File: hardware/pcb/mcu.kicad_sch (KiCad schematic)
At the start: 14 parts, among them J3 FSR pads, U1 ESP32-WROOM-32E-N8R2, U18 W25Q512JVEIQ, U19 TCA6408ARSVR

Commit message: Fix the review's datasheet errors without changing respiration or the GDTs.
Replace the MCP73831 with a BQ25170 so a flat cell still charges from USB, add the missing series protection and ESP32/CP2102 passives, and withdraw the claim that respiration still works with 51 kΩ in the loop.

Co-authored-by: Riyu-D1 <Riyu-D1@users.noreply.github.com>
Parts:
- added C64: 1u, Capacitor_SMD:C_0402_1005Metric, symbol vitalq:C
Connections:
- net +3V3: no longer U19.1 (~{RESET})
- net ESP_EN: now also U19.1 (~{RESET}), C64.1
- net GND: now also C64.2
- net GAUGE_ALRT: now reaches U1.10 (IO25)
- net CHG_PG: now reaches U1.12 (IO27)
- net CHG_EN renamed CHG_DIS
- net NTC_ADC: no longer names the net of U1.5 (SENSOR_VN)
- no-connect marks 5 -> 4
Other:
- note added: "EN has R5 10k and C64 1 uF. Q3 on the USB sheet is the DTR/RTS auto-program pair."
- note removed: "EN and IO0 have pull-ups only. Download uses the module pads. There are no buttons."

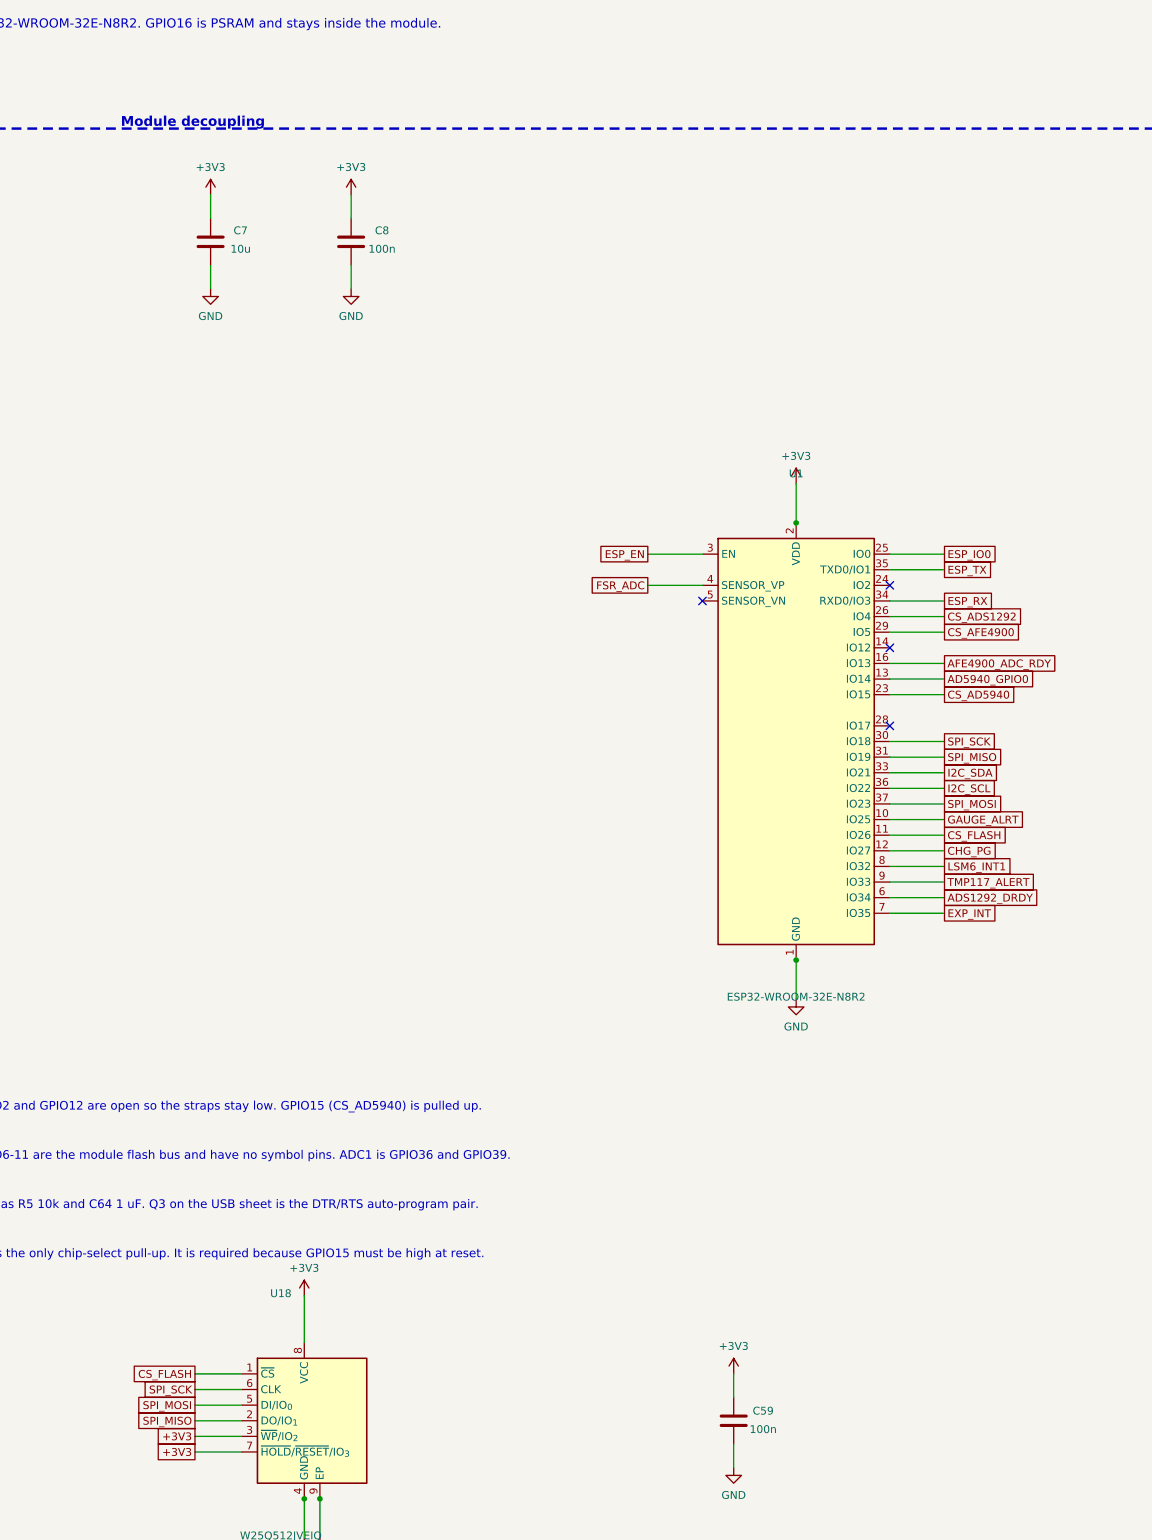
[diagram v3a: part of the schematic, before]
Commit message: Prepare hw_v1 for prefab review without claiming the route is finished.
Add the gauge TDFN, USB ESD, sense links, test access, and JLC BOM fields, and keep the partial Freerouting result with the remaining open nets listed.

Co-authored-by: Riyu-D1 <Riyu-D1@users.noreply.github.com>
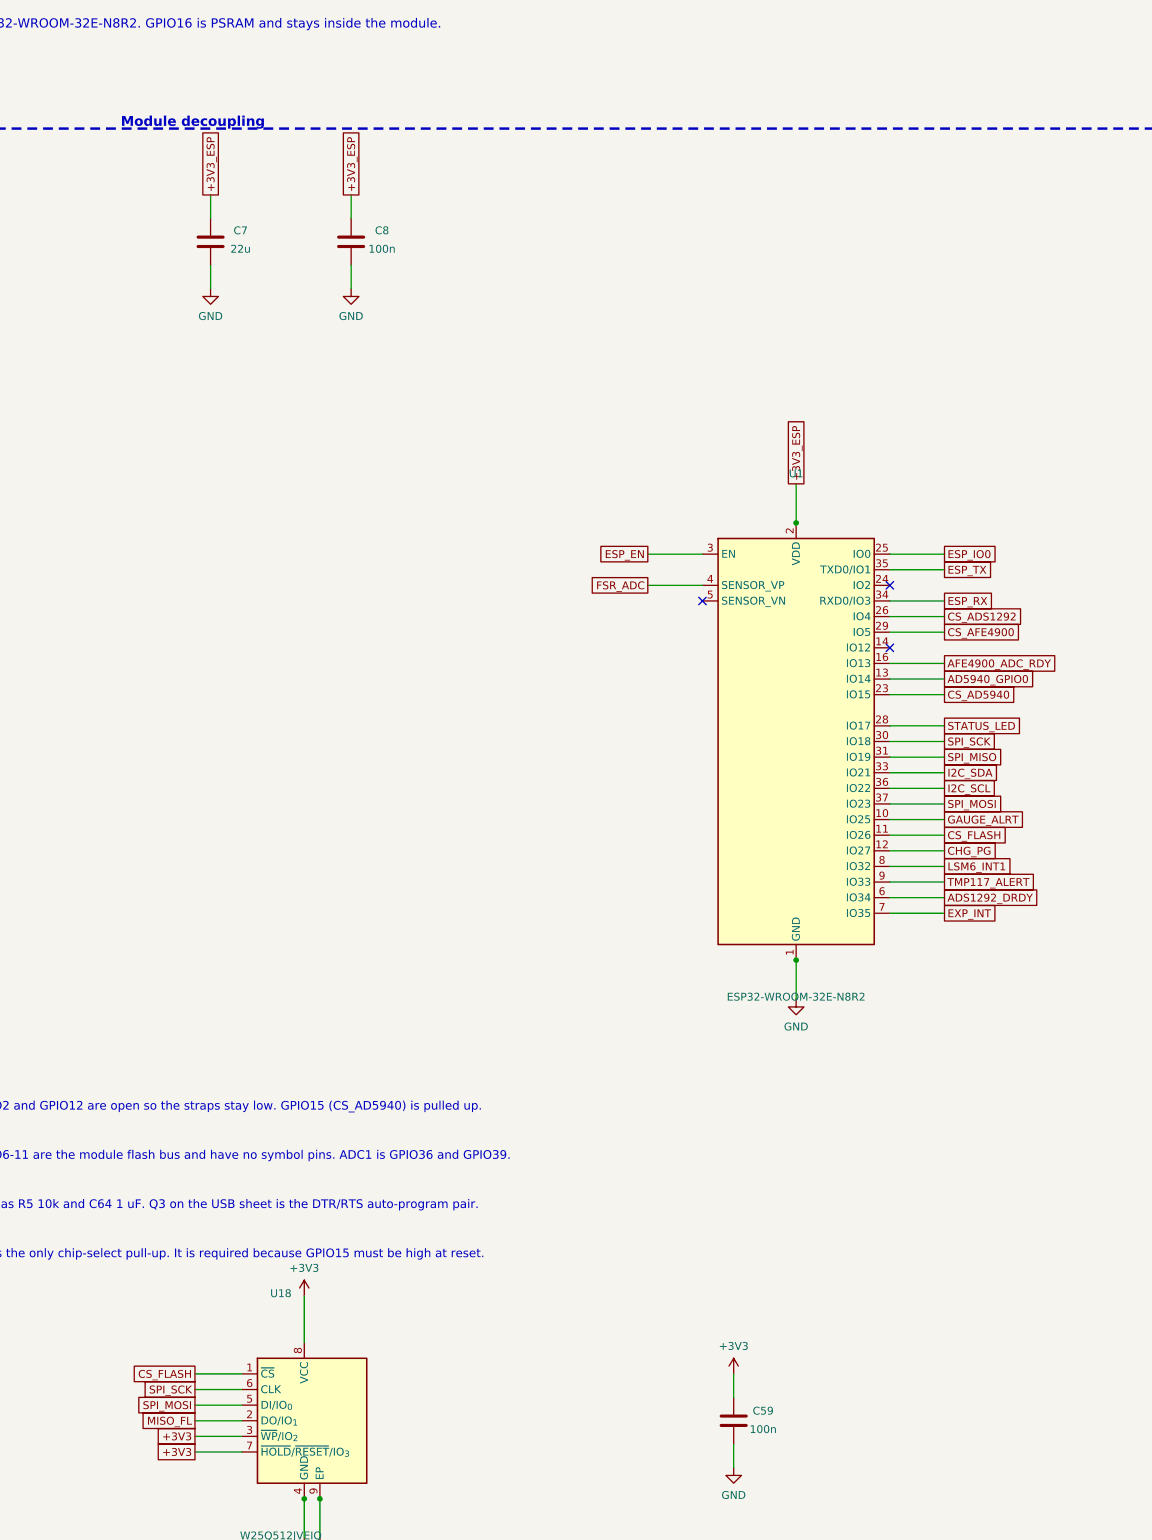
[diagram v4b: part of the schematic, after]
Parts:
- C7: value 10u -> 22u; footprint Capacitor_SMD:C_0402_1005Metric -> Capacitor_SMD:C_0603_1608Metric
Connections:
- net +3V3: no longer C7.1, C8.1, U1.2 (VDD)
- net SPI_MISO: no longer U18.2 (DO/IO_{1})
- net STATUS_LED: now reaches U1.28 (IO17)
- new net +3V3_ESP: C7.1, C8.1, U1.2 (VDD)
- new net MISO_FL: U18.2 (DO/IO_{1})
- no-connect marks 4 -> 3
